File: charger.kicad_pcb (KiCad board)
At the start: 2 copper layers, 115 parts, among them J1 XUNPU DC-005-A250, Q2 AM2302N-T1-PF-VB, Q3 AM2302N-T1-PF-VB, Q4 AM2302N-T1-PF-VB, Q5 AM2302N-T1-PF-VB, Q6 AM2302N-T1-PF-VB, U2 DSIC08LSGET_C3293158, U4 EUP3489WIR1, U5 EUP3489WIR1, U6 EUP3489WIR1, U7 EUP3489WIR1, U8 EUP3489WIR1

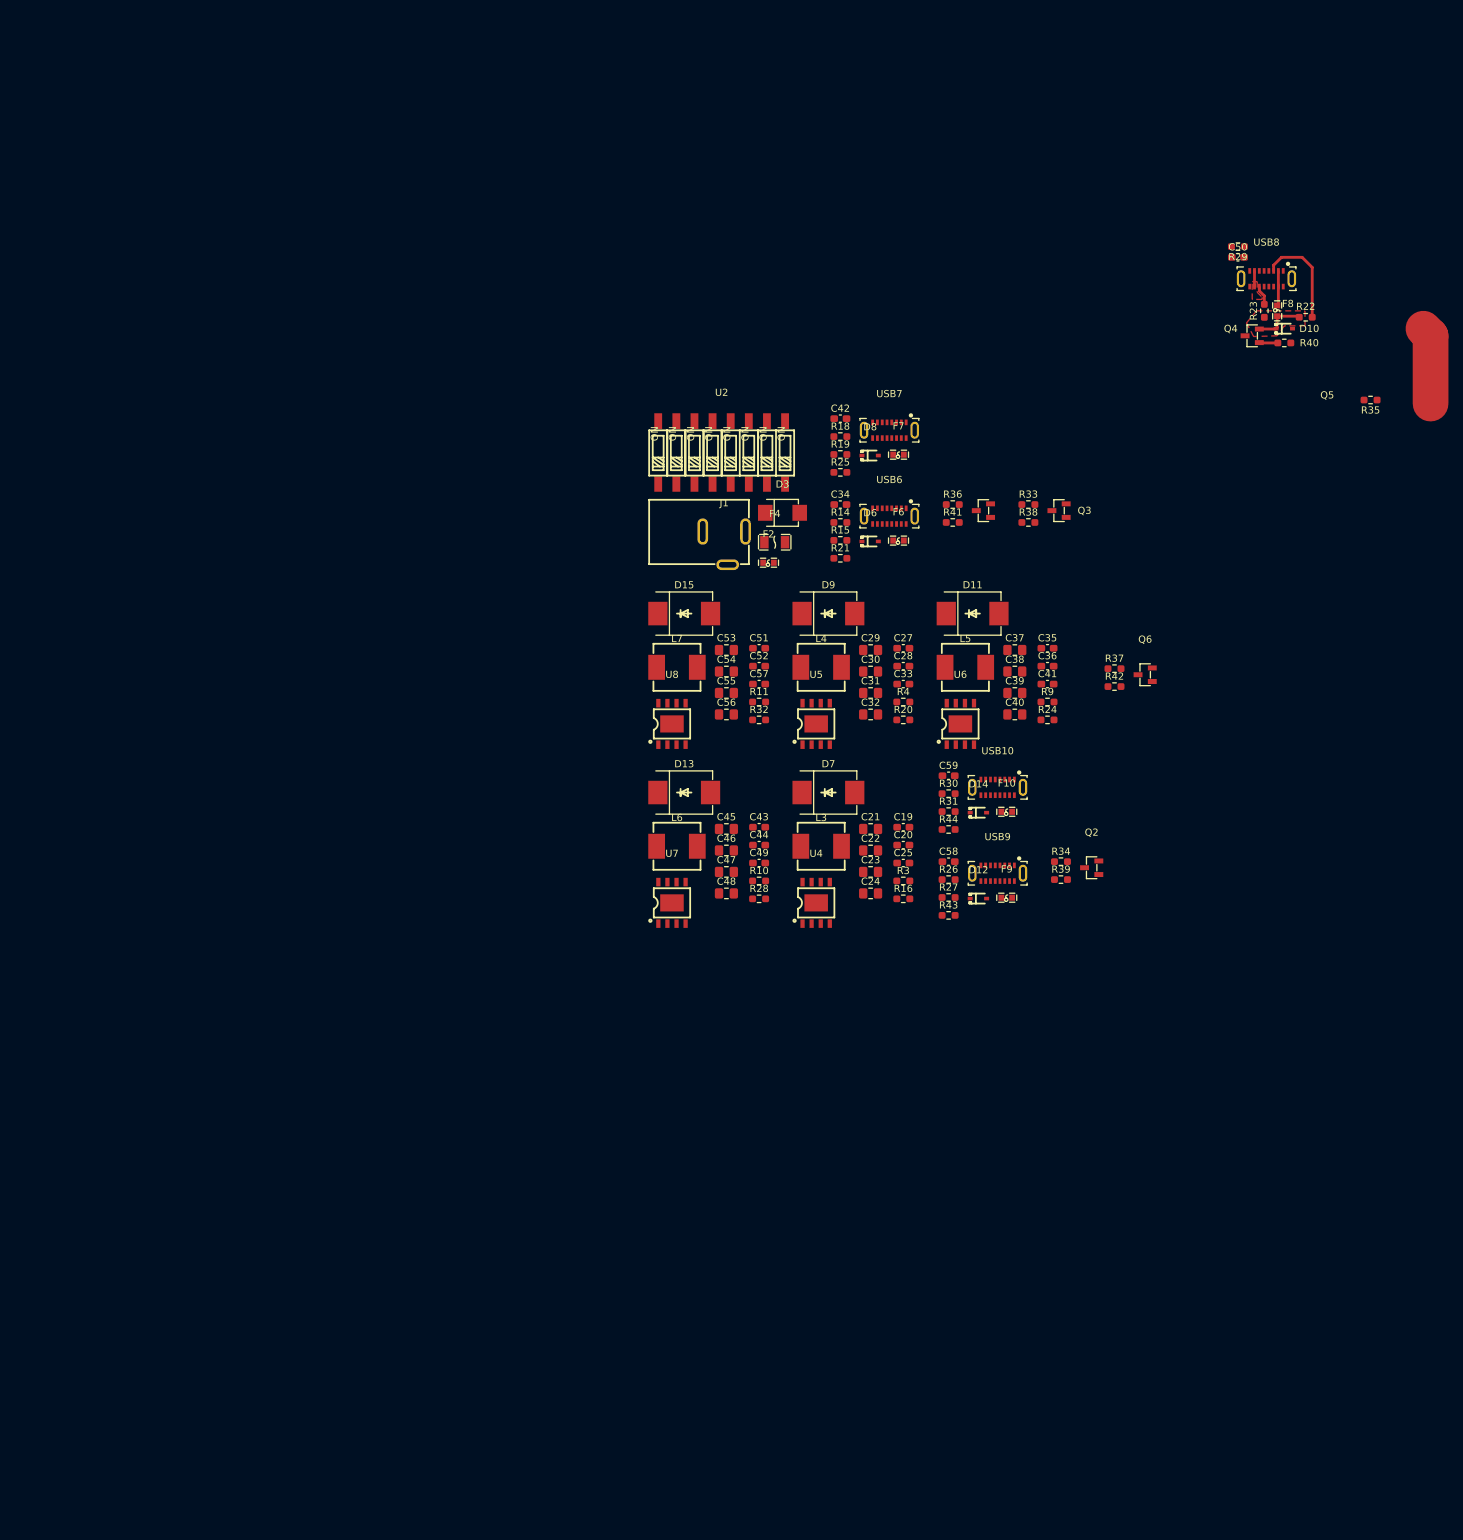
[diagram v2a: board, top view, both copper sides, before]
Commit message: routing and layout done except spacing and final power route
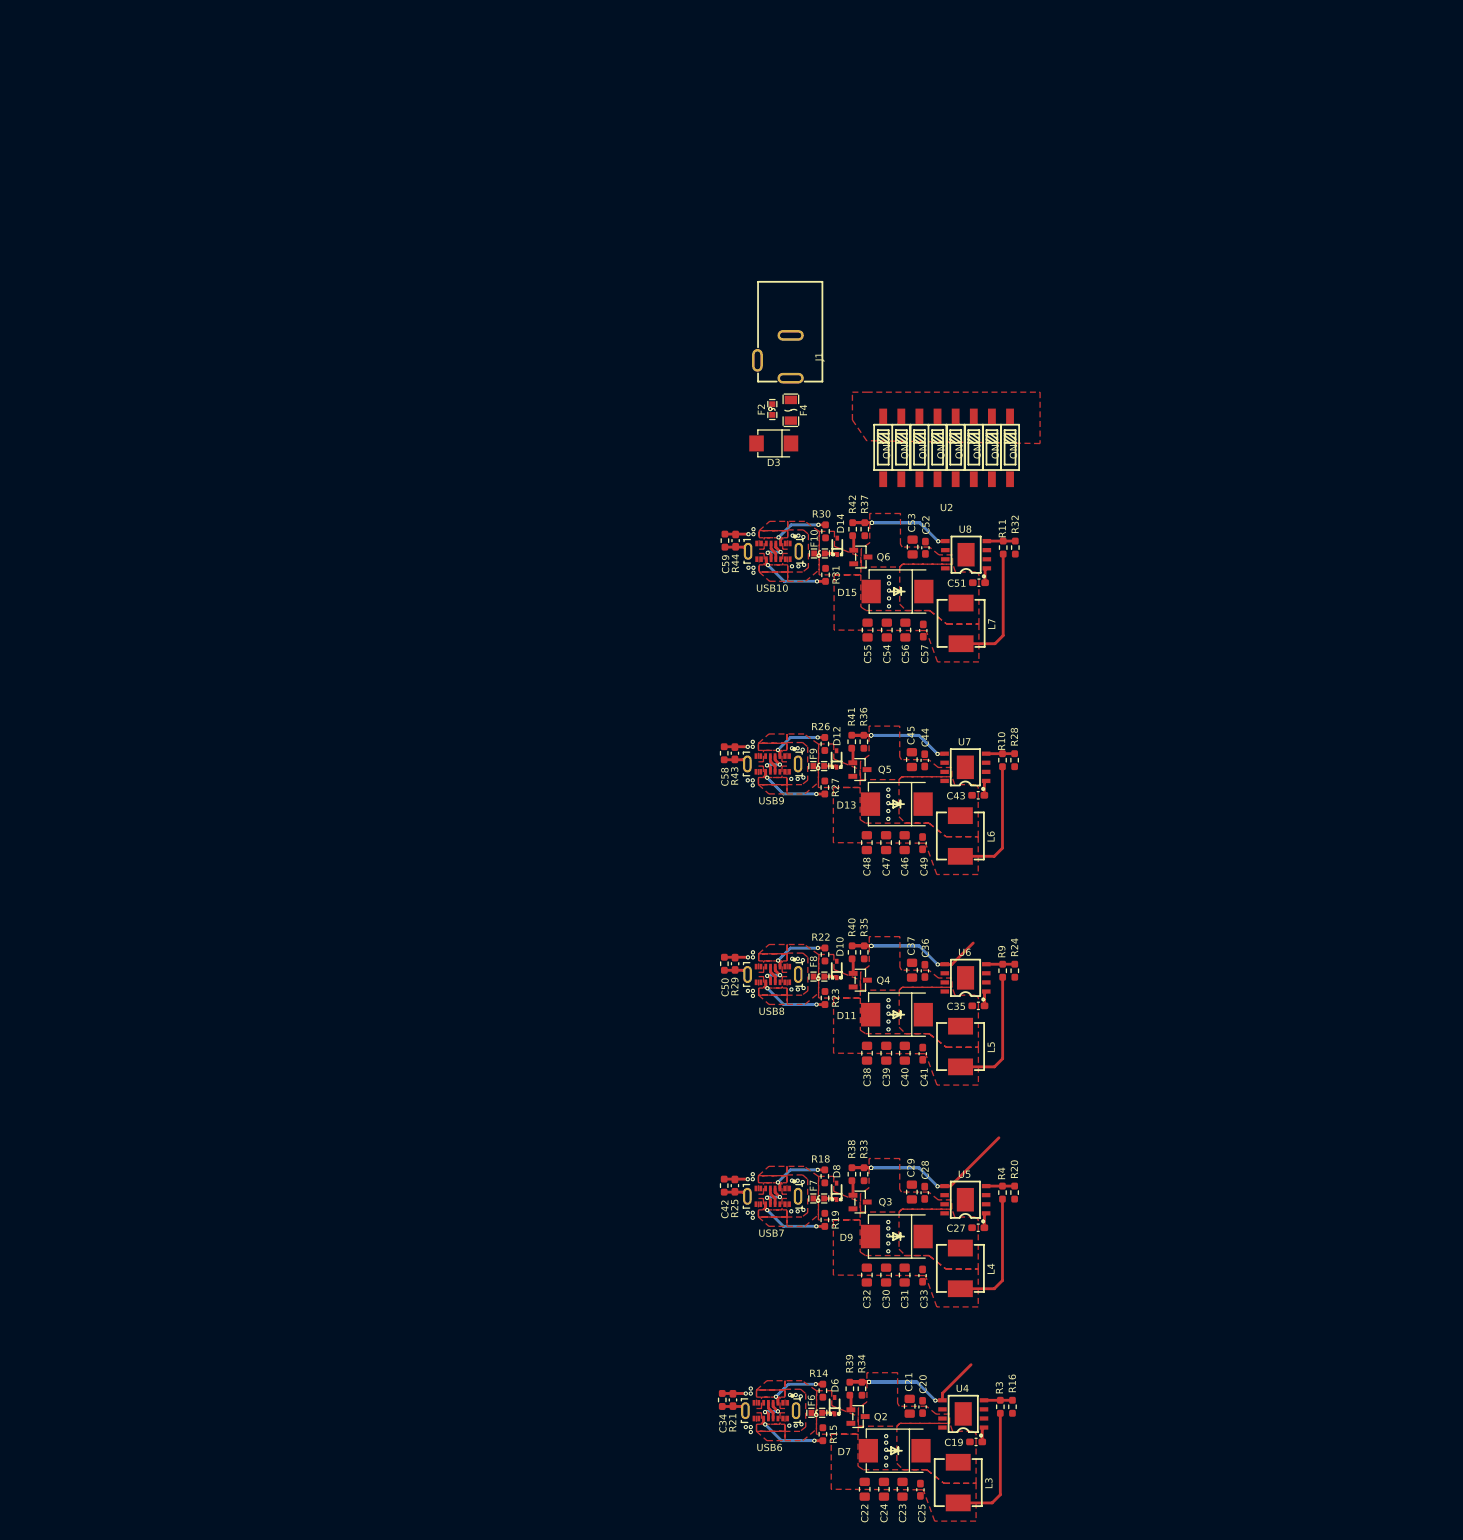
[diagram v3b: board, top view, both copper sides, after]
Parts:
- moved USB6 126.5 mm to (106.0, 179.6)
- moved C34 126.4 mm to (100.7, 178.1), turned to 90 degrees
- moved R15 125.3 mm to (113.3, 182.9), turned to 90 degrees
- moved R29 123.6 mm to (99.5, 117.0), turned to -90 degrees
- moved F6 122.8 mm to (112.5, 179.9)
- moved R14 121.7 mm to (113.3, 176.8), turned to -90 degrees
- moved C50 121.5 mm to (101.0, 117.0), turned to 90 degrees
- moved D6 121.2 mm to (115.0, 178.9), turned to 90 degrees
- moved USB8 119.6 mm to (106.3, 118.5)
- moved R21 119.1 mm to (99.2, 178.1), turned to -90 degrees
- moved R23 114.3 mm to (113.6, 121.8), turned to 90 degrees
- moved F8 113.3 mm to (112.8, 118.8), turned to 0 degrees
- moved R22 111.9 mm to (113.6, 115.7), turned to -90 degrees
- moved D10 109.5 mm to (115.3, 117.8), turned to 90 degrees
- moved USB7 108.6 mm to (106.3, 149.6)
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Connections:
- R10 pad 2: Net-(R10-Pad2) -> Net-(U7-FB)
- R11 pad 2: Net-(R11-Pad2) -> Net-(U8-FB)
- R16 pad 1: Net-(R16-Pad1) -> Net-(U4-FB)
- R20 pad 1: Net-(R20-Pad1) -> Net-(U5-FB)
- R24 pad 1: Net-(R24-Pad1) -> Net-(U6-FB)
- R28 pad 1: Net-(R10-Pad2) -> Net-(U7-FB)
- R3 pad 2: Net-(R16-Pad1) -> Net-(U4-FB)
- R32 pad 1: Net-(R11-Pad2) -> Net-(U8-FB)
- R4 pad 2: Net-(R20-Pad1) -> Net-(U5-FB)
- R9 pad 2: Net-(R24-Pad1) -> Net-(U6-FB)
- U4 pad 4: /REG_USB/Enable -> Net-(U4-FB)
- U4 pad 5: unconnected-(U4-EN-Pad5) -> /REG_USB/Enable
- U5 pad 4: /REG_USB1/Enable -> Net-(U5-FB)
- U5 pad 5: unconnected-(U5-EN-Pad5) -> /REG_USB1/Enable
- U6 pad 4: /REG_USB2/Enable -> Net-(U6-FB)
- U6 pad 5: unconnected-(U6-EN-Pad5) -> /REG_USB2/Enable
- U7 pad 4: /REG_USB3/Enable -> Net-(U7-FB)
- U7 pad 5: unconnected-(U7-EN-Pad5) -> /REG_USB3/Enable
- U8 pad 4: /REG_USB4/Enable -> Net-(U8-FB)
- U8 pad 5: unconnected-(U8-EN-Pad5) -> /REG_USB4/Enable
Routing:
- net /REG_USB1/Enable: track 0.00 -> 33.9 mm, vias 0 -> 3
- net /REG_USB/Enable: track 0.00 -> 30.1 mm, vias 0 -> 3
- net /REG_USB2/Enable: track 0.00 -> 29.7 mm, vias 0 -> 3
- net /REG_USB4/Enable: track 0.00 -> 23.5 mm, vias 0 -> 3
- net /REG_USB3/Enable: track 0.00 -> 23.5 mm, vias 0 -> 3
- net /REG_USB4/USB receptacle2/VBUS: track 0.00 -> 20.1 mm
- net /REG_USB/USB receptacle2/VBUS: track 0.00 -> 20.1 mm
- net /REG_USB1/USB receptacle2/VBUS: track 0.00 -> 20.1 mm
- net /REG_USB3/USB receptacle2/VBUS: track 0.00 -> 20.1 mm
- net GND: track 0.00 -> 16.5 mm, vias 0 -> 85
- net /REG_USB2/USB receptacle2/VBUS: track 7.54 -> 20.1 mm
- net (no net): track 10.9 -> 0.00 mm
- net Net-(USB9-CC2): track 0.00 -> 9.94 mm, vias 0 -> 2
- net Net-(USB10-CC2): track 0.00 -> 9.94 mm, vias 0 -> 2
- net Net-(USB7-CC2): track 0.00 -> 9.94 mm, vias 0 -> 2
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- added copper zone on F.Cu, net /REG_USB/USB receptacle2/VBUS
- added copper zone on F.Cu, net /REG_USB/USB receptacle2/Vusb_no_f
- added copper zone on F.Cu, net /REG_USB1/USB receptacle2/VBUS
- added copper zone on F.Cu, net /REG_USB1/USB receptacle2/Vusb_no_f
- added copper zone on F.Cu, net /REG_USB2/USB receptacle2/VBUS
- added copper zone on F.Cu, net /REG_USB3/USB receptacle2/VBUS
- added copper zone on F.Cu, net /REG_USB3/USB receptacle2/Vusb_no_f
- added copper zone on F.Cu, net /REG_USB4/USB receptacle2/VBUS
- added copper zone on F.Cu, net /REG_USB4/USB receptacle2/Vusb_no_f
- added copper zone on F.Cu, net /Vin
- added copper zone on F.Cu, net Net-(D11-C)
- added copper zone on F.Cu, net Net-(D13-C)
- added copper zone on F.Cu, net Net-(D15-C)
- added copper zone on F.Cu, net Net-(D7-C)
- added copper zone on F.Cu, net Net-(D9-C)
